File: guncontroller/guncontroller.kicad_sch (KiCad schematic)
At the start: 22 parts, among them SW1 SW_Push, SW2 SW_Push, SW3 SW_Push, SW4 SW_Push, SW5 SW_Push, SW6 SW_Push, SW7 SW_Push, SW8 SW_Push, U1 MPU-6050

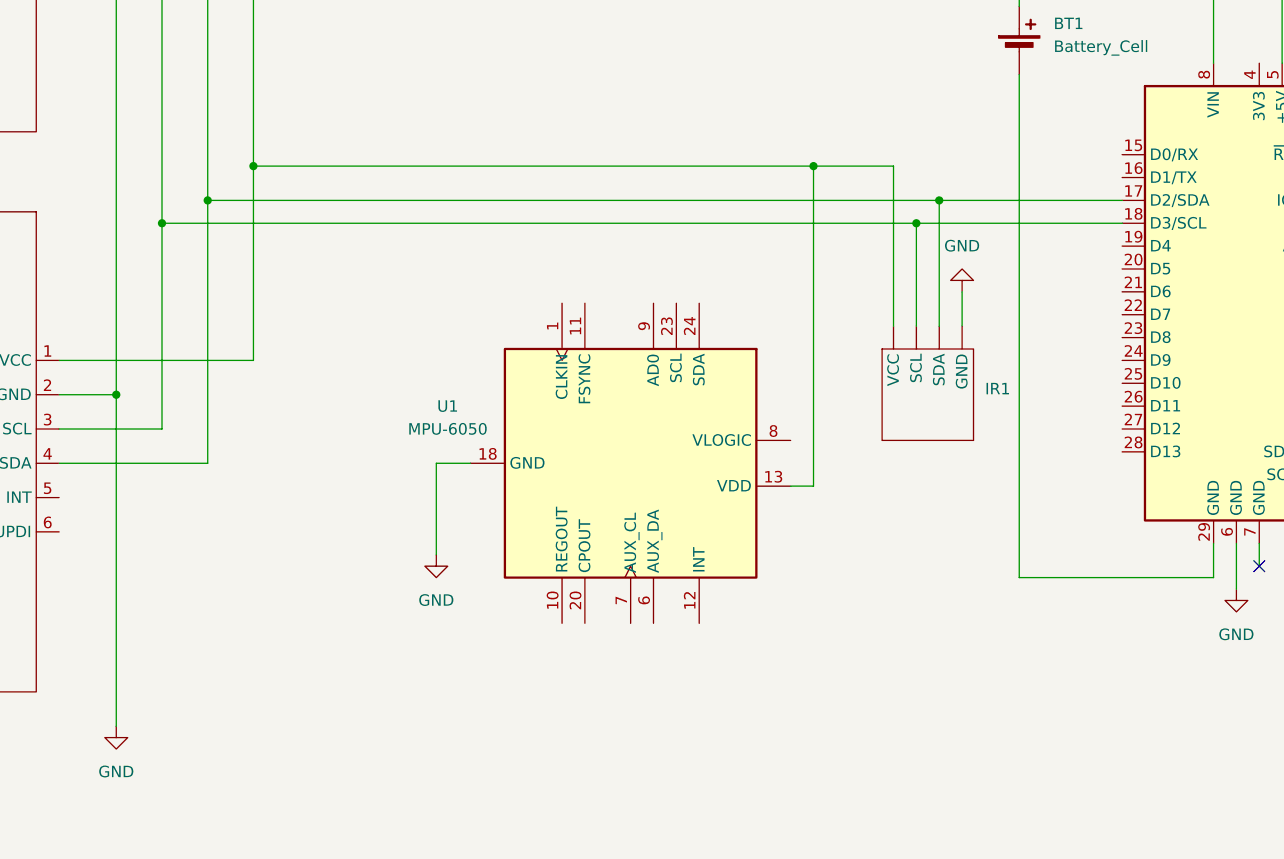
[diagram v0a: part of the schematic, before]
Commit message: Changed SCL wire color and added trigger buttons
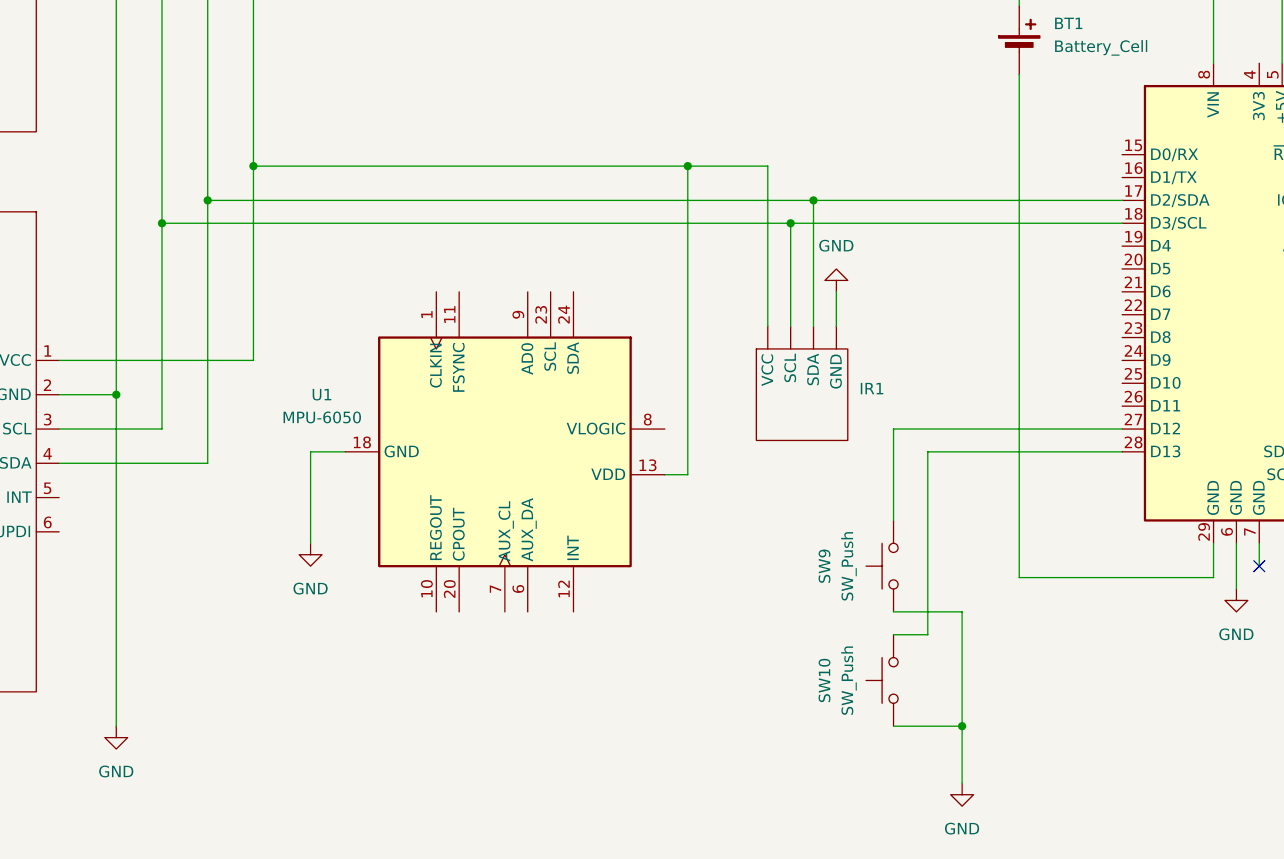
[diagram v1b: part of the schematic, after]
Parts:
- added SW10, SW9: SW_Push, symbol Switch:SW_Push
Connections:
- net GND: now also SW10.1, SW9.1
- net at A1.27 (D12): now also SW9.2
- net at A1.28 (D13): now also SW10.2
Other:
- moved on the sheet: IR1, U1

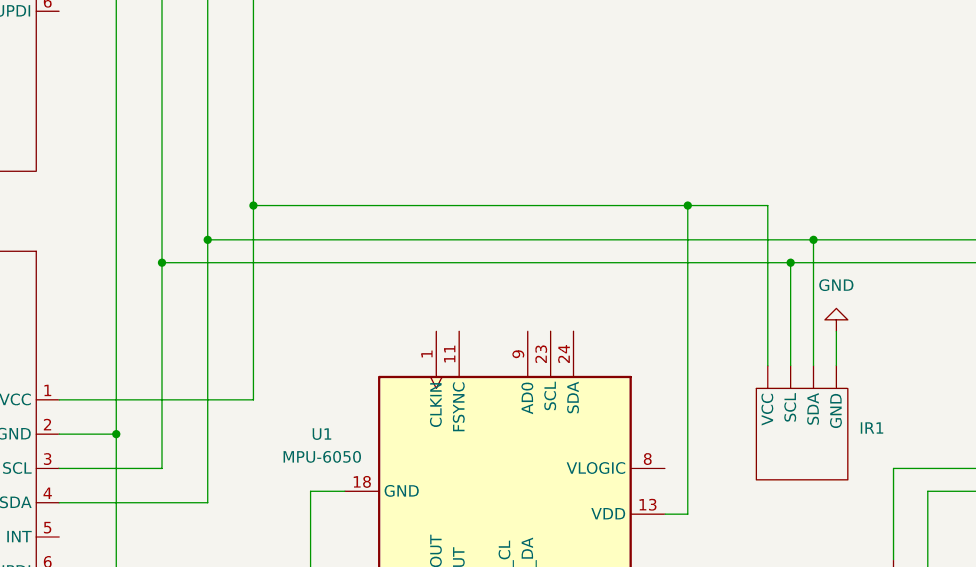
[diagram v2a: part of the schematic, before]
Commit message: Fixed accelerometer not being connected to i2c in schematic
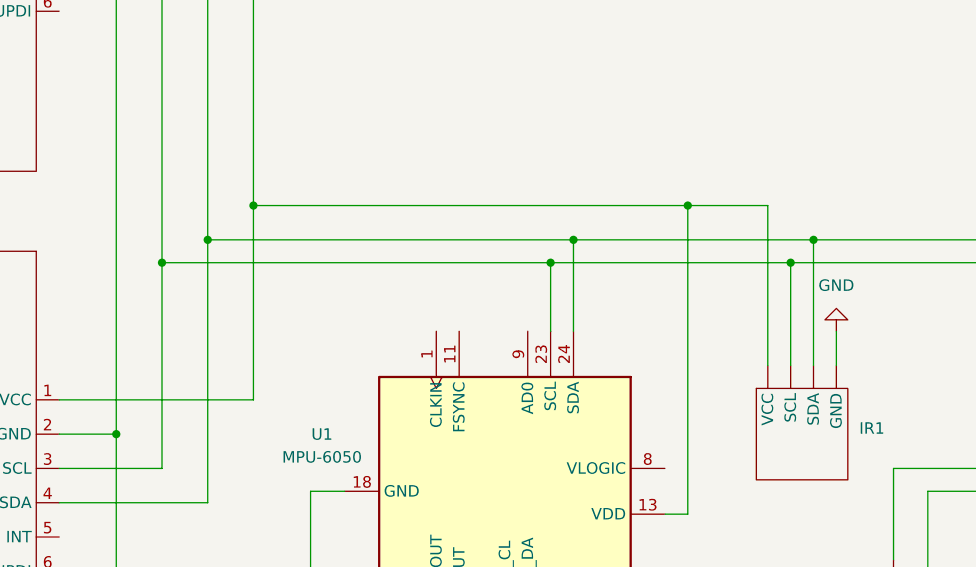
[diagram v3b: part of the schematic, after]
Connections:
- net at U1.23 (SCL): now also A1.18 (D3/SCL), BB1.3 (SCL), BB2.3 (SCL), IR1. (VCC)
- net at U1.24 (SDA): now also A1.17 (D2/SDA), BB1.4 (SDA), BB2.4 (SDA), IR1. (VCC)
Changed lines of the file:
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@@
+	)
+	(junction
+		(at 156.21 86.36)
+		(diameter 0)
+		(color 255 237 0 1)
 	)
 	(junction
@@
 	)
 	(junction
+		(at 153.67 88.9)
+		(diameter 0)
+		(color 255 124 232 1)
+	)
+	(junction
 		(at 110.49 88.9)
 		(diameter 0)
@@
 	(wire
 		(pts
-			(xy 180.34 88.9) (xy 110.49 88.9)
+			(xy 156.21 86.36) (xy 156.21 96.52)
+		)
+		(stroke
+			(width 0)
+			(type default)
+			(color 255 232 0 1)
+		)
+	)
+	(wire
+		(pts
+			(xy 180.34 88.9) (xy 153.67 88.9)
 		)
 		(stroke
@@
 	(wire
 		(pts
+			(xy 153.67 88.9) (xy 153.67 96.52)
+		)
+		(stroke
+			(width 0)
+			(type default)
+			(color 255 122 208 1)
+		)
+	)
+	(wire
+		(pts
 			(xy 168.91 82.55) (xy 120.65 82.55)
 		)
@@
 	(wire
 		(pts
+			(xy 156.21 86.36) (xy 115.57 86.36)
+		)
+		(stroke
+			(width 0)
+			(type default)
+			(color 255 232 0 1)
+		)
+	)
+	(wire
+		(pts
 			(xy 87.63 74.93) (xy 62.23 74.93)
 		)
@@
 	(wire
 		(pts
+			(xy 153.67 88.9) (xy 110.49 88.9)
+		)
+		(stroke
+			(width 0)
+			(type default)
+			(color 255 122 208 1)
+		)
+	)
+	(wire
+		(pts
 			(xy 242.57 81.28) (xy 245.11 81.28)
 		)
@@
 	(wire
 		(pts
-			(xy 182.88 86.36) (xy 115.57 86.36)
+			(xy 182.88 86.36) (xy 156.21 86.36)
 		)
 		(stroke
@@
 	)
 	(symbol
-		(lib_name "GunProject_lib:ButtonBreakout")
 		(lib_id "GunProject_lib:ButtonBreakout")
 		(at 87.63 114.3 270)

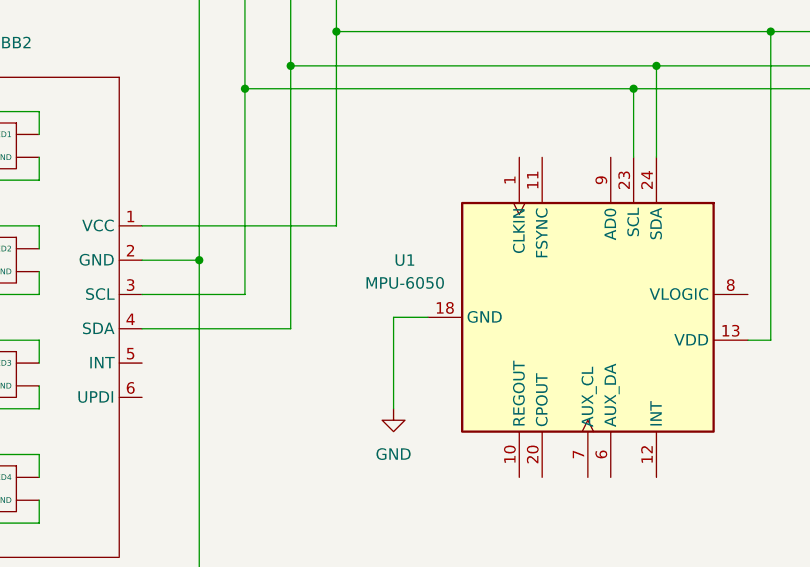
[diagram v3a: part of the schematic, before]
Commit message: Changed accelerometer to BNO055 changed Arcade button wires
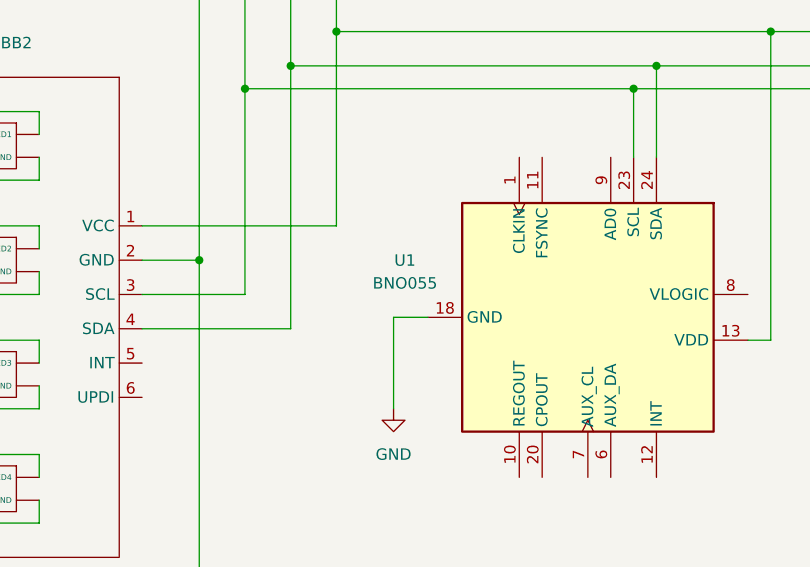
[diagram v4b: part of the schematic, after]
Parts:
- U1: value MPU-6050 -> BNO055
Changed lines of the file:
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@@
 			(width 0)
 			(type default)
-			(color 1 0 255 1)
 		)
 	)
@@
 			(width 0)
 			(type default)
-			(color 1 0 255 1)
 		)
 	)
@@
 			(width 0)
 			(type default)
-			(color 1 0 255 1)
 		)
 	)
@@
 			(width 0)
 			(type default)
-			(color 255 0 13 1)
 		)
 	)
@@
 			(width 0)
 			(type default)
-			(color 1 0 255 1)
 		)
 	)
@@
 			(width 0)
 			(type default)
-			(color 1 0 255 1)
 		)
 	)
@@
 			(width 0)
 			(type default)
-			(color 1 0 255 1)
 		)
 	)
@@
 			(width 0)
 			(type default)
-			(color 1 0 255 1)
 		)
 	)
@@
 			(width 0)
 			(type default)
-			(color 255 0 13 1)
 		)
 	)
@@
 			(width 0)
 			(type default)
-			(color 1 0 255 1)
 		)
 	)
@@
 			(width 0)
 			(type default)
-			(color 1 0 255 1)
 		)
 	)
@@
 			(width 0)
 			(type default)
-			(color 255 0 13 1)
 		)
 	)
@@
 			(width 0)
 			(type default)
-			(color 1 0 255 1)
 		)
 	)
@@
 			(width 0)
 			(type default)
-			(color 1 0 255 1)
 		)
 	)
@@
 			(width 0)
 			(type default)
-			(color 255 0 13 1)
 		)
 	)
@@
 			(width 0)
 			(type default)
-			(color 255 0 13 1)
 		)
 	)
@@
 			(width 0)
 			(type default)
-			(color 1 0 255 1)
 		)
 	)
@@
 			(width 0)
 			(type default)
-			(color 1 0 255 1)
 		)
 	)
@@
 			(width 0)
 			(type default)
-			(color 255 0 13 1)
 		)
 	)
@@
 			(width 0)
 			(type default)
-			(color 1 0 255 1)
 		)
 	)
@@
 			(width 0)
 			(type default)
-			(color 255 0 13 1)
 		)
 	)
@@
 			(width 0)
 			(type default)
-			(color 1 0 255 1)
 		)
 	)
@@
 			(width 0)
 			(type default)
-			(color 1 0 255 1)
 		)
 	)
@@
 			(width 0)
 			(type default)
-			(color 1 0 255 1)
 		)
 	)
@@
 			(width 0)
 			(type default)
-			(color 1 0 255 1)
 		)
 	)
@@
 			(width 0)
 			(type default)
-			(color 255 0 13 1)
 		)
 	)
@@
 			(width 0)
 			(type default)
-			(color 1 0 255 1)
 		)
 	)
@@
 			(width 0)
 			(type default)
-			(color 1 0 255 1)
 		)
 	)
@@
 			(width 0)
 			(type default)
-			(color 1 0 255 1)
 		)
 	)
@@
 			(width 0)
 			(type default)
-			(color 1 0 255 1)
 		)
 	)
@@
 			(width 0)
 			(type default)
-			(color 1 0 255 1)
 		)
 	)
@@
 			(width 0)
 			(type default)
-			(color 255 0 13 1)
 		)
 	)
@@
 			(width 0)
 			(type default)
-			(color 1 0 255 1)
 		)
 	)
@@
 			(width 0)
 			(type default)
-			(color 1 0 255 1)
 		)
 	)
@@
 			(width 0)
 			(type default)
-			(color 1 0 255 1)
 		)
 	)
@@
 			(width 0)
 			(type default)
-			(color 255 0 13 1)
 		)
 	)
@@
 			(width 0)
 			(type default)
-			(color 255 0 13 1)
 		)
 	)
@@
 			(width 0)
 			(type default)
-			(color 255 0 13 1)
 		)
 	)
@@
 			(width 0)
 			(type default)
-			(color 1 0 255 1)
 		)
 	)
@@
 			(width 0)
 			(type default)
-			(color 1 0 255 1)
 		)
 	)
@@
 			(width 0)
 			(type default)
-			(color 255 0 13 1)
 		)
 	)
@@
 			(width 0)
 			(type default)
-			(color 1 0 255 1)
 		)
 	)
@@
 			(width 0)
 			(type default)
-			(color 1 0 255 1)
 		)
 	)
@@
 			(width 0)
 			(type default)
-			(color 255 0 13 1)
 		)
 	)
@@
 			(width 0)
 			(type default)
-			(color 255 0 13 1)
 		)
 	)
@@
 			(width 0)
 			(type default)
-			(color 1 0 255 1)
 		)
 	)
@@
 			(width 0)
 			(type default)
-			(color 1 0 255 1)
 		)
 	)
@@
 			(width 0)
 			(type default)
-			(color 255 0 13 1)
 		)
 	)
@@
 			)
 		)
-		(property "Value" "MPU-6050"
+		(property "Value" "BNO055"
 			(at 128.27 110.5214 90)
 			(effects
